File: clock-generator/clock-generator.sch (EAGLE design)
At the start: 100 parts, among them IC1 24C00TS, K2 694108106102, M1 MENTOR_12701001, U1 SN74LVC1G04DBV, U2 ADP151AUJZ, U3 ATSAMD21E, U4 SI5351C, U5 IP4234CZ6, U6 IP4234CZ6, X1 MINI-USB-SHIELD-UX60A-MB-5ST, X2 JACK2.5_SJ-2523, X4 UEXT/90

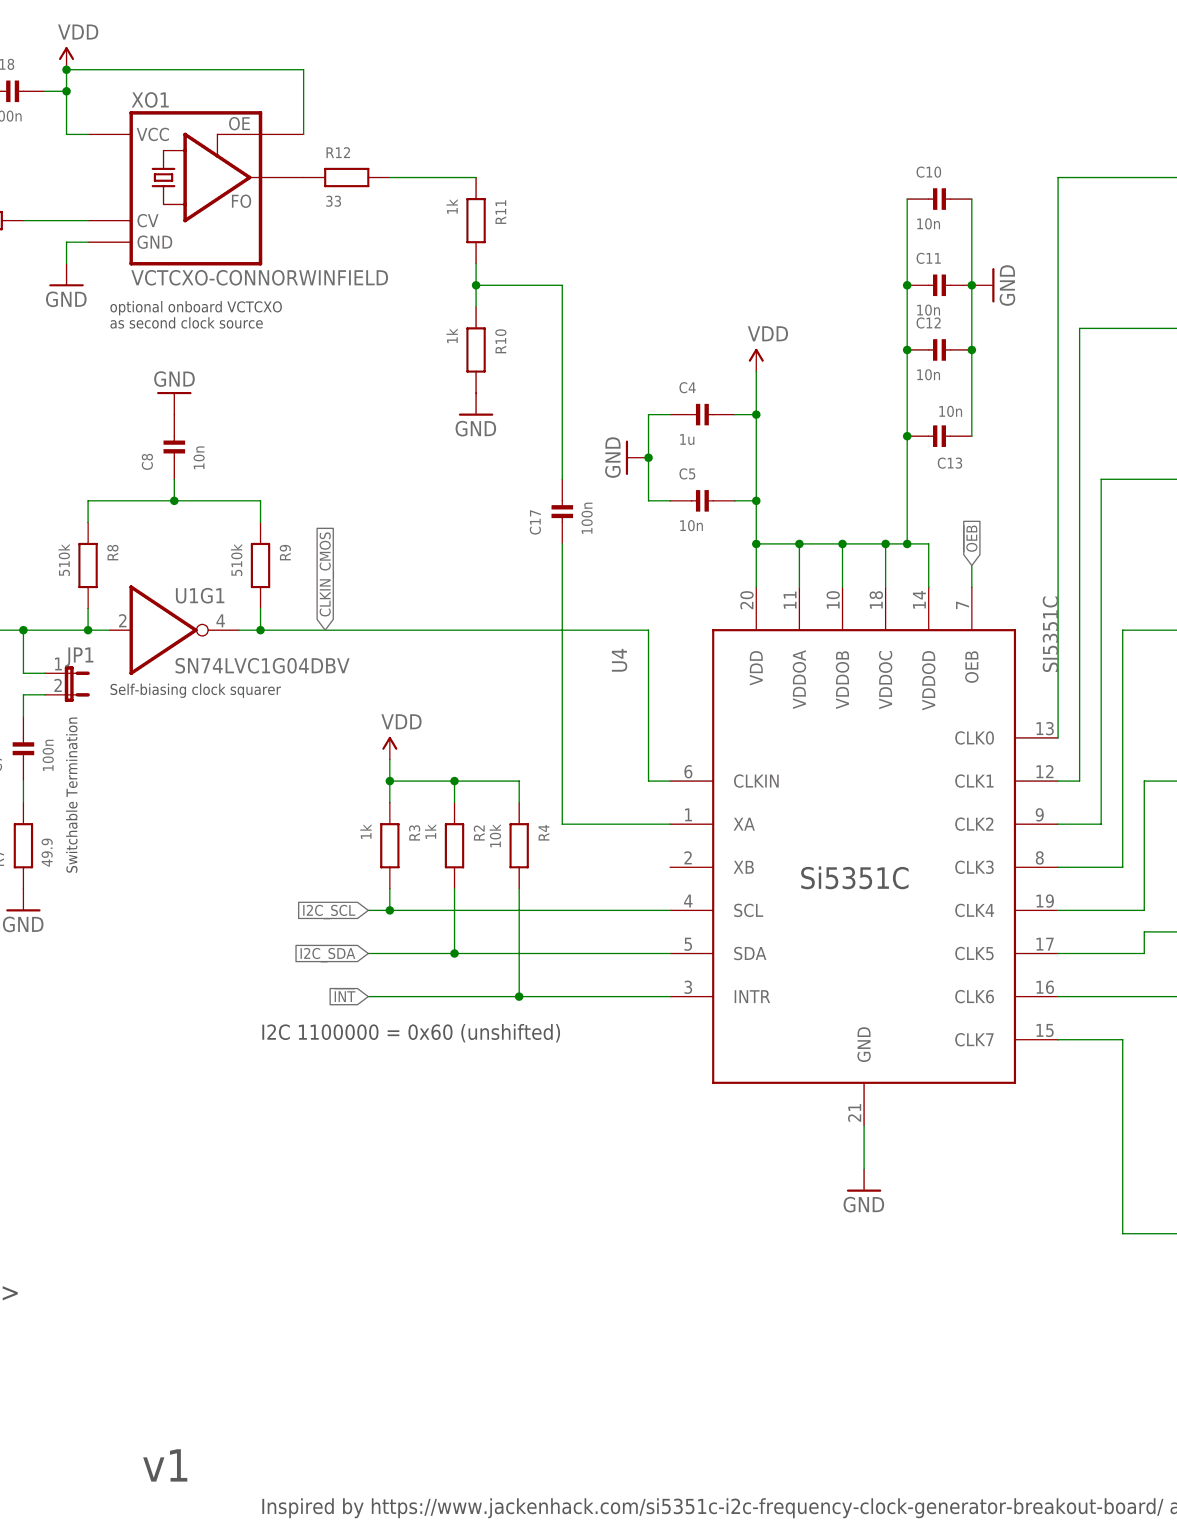
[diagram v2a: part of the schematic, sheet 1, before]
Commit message: clock-generator: add tracking LDO, make PCB four layer
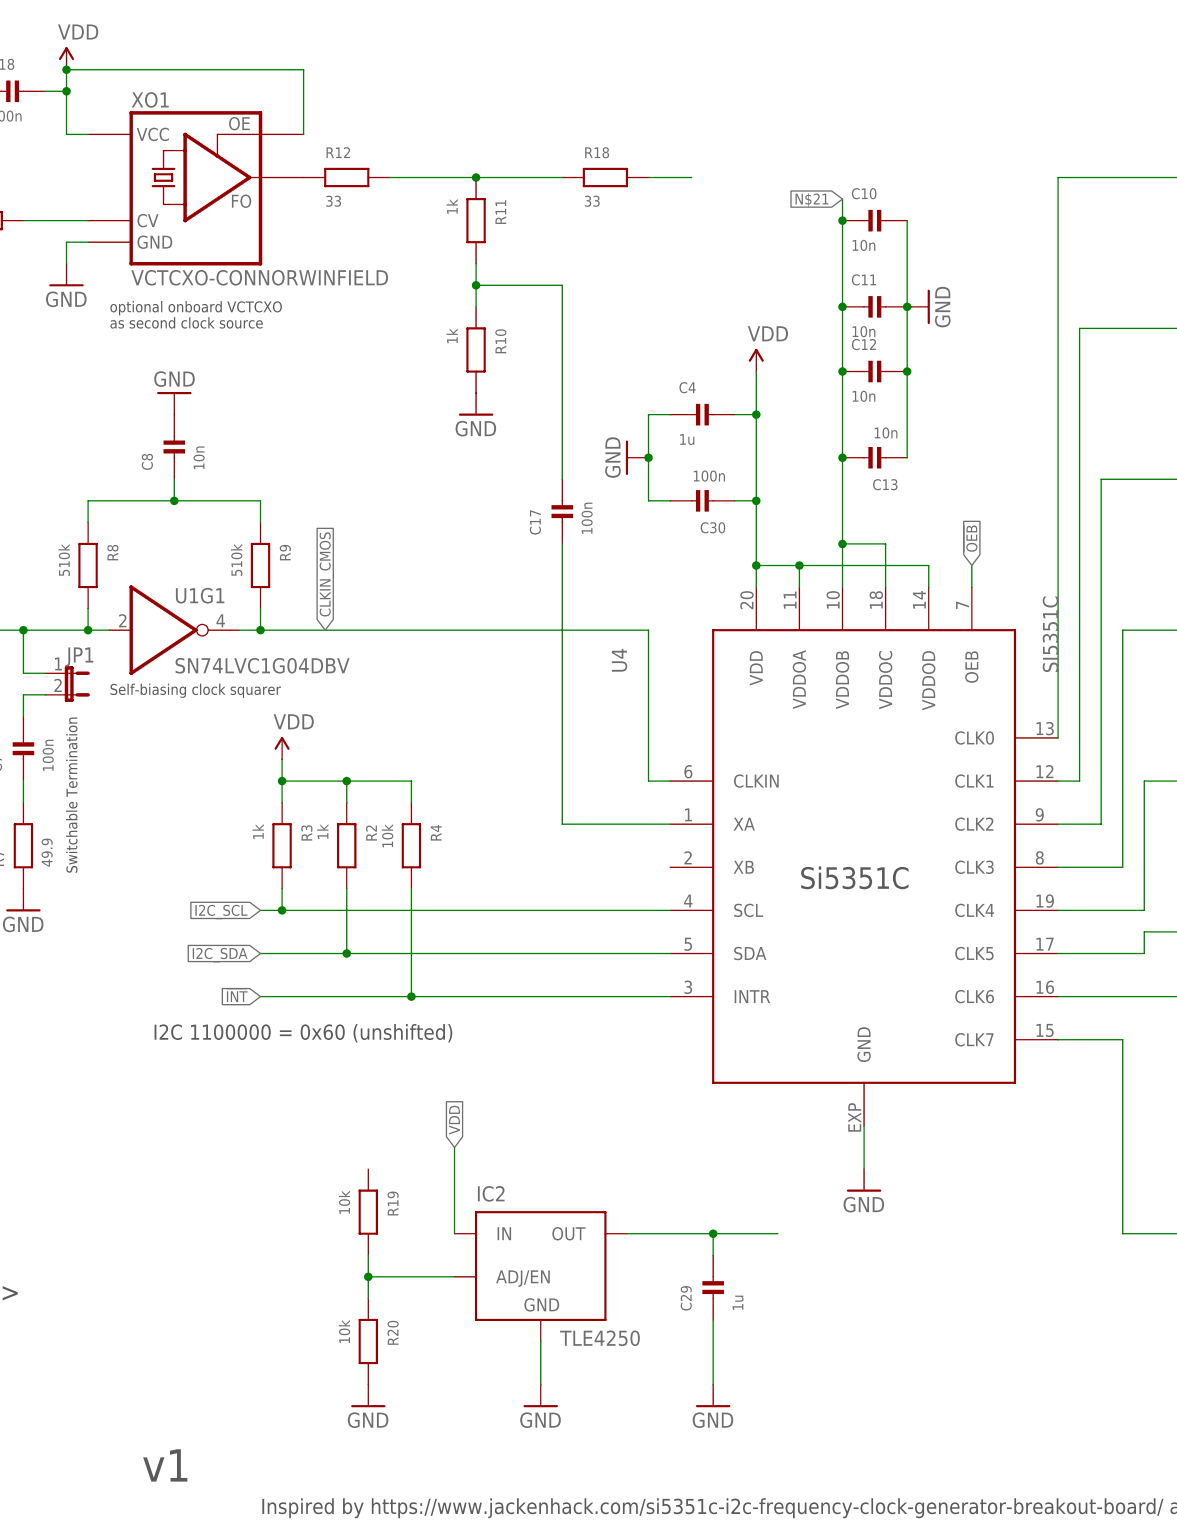
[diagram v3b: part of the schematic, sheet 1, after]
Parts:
- removed C5: 10n, rc-sysmocom:CAP_CERAMIC_0402
- added C29: 1u, rc-sysmocom:CAP_CERAMIC_0603
- added C30: 100n, rc-sysmocom:CAP_CERAMIC_0603
- added IC2: TLE4250, TLE4250:TLE4250
- added R18: 33, rc-sysmocom:RESISTOR_0603
- added R19, R20: 10k, rc-sysmocom:RESISTOR_0603
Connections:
- new net N$17: R18.2
- new net N$18: U3.PA10/AIN18/X2/SC0P2/SC2P2/TCC1WO0/TCC0WO2/I2S_SCK0/GCLK_IO4
- new net N$19: C29.2, IC2.OUT
- new net N$20: IC2.ADJ/EN, R19.2, R20.1
- new net N$21: C10.1, C11.1, C12.1, C13.2, U4.VDDOB, U4.VDDOC
- new net N$8: U3.PA28/TCC3WO7/GCLK_IO0
- new net UART_RX1: U3.PA01/SC1P1/TCC2WO1, X4.RXD
- new net UART_TX1: U3.PA00/SC1P0/TCC2WO0, X4.TXD
- net GND: now also C29.1, C30.2, IC2.GND, R20.2; no longer C5.1
- net N$1: now also R18.1
- net SWCLK: no longer U3.PA30/SC1P2/TCC1WO0/TCC3WO4/SWCLK/GCLK_IO0
- net UART_RX0: no longer X4.RXD
- net UART_TX0: no longer X4.TXD
- net VDD: now also C30.1, IC2.IN; no longer C10.1, C11.1, C12.1, C13.2, C5.2, U4.VDDOB, U4.VDDOC
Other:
- moved on the sheet: C10, C11, C12, C13, R2, R3, R4, U4

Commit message: clock-generator: insert changes discussed so far for v2
* selectable VDDIO{1..4} for PLL: either 3V3 or ADJ (VOUT/DAC)
* use SAMD21 instead of SAMD11
* bring some GPIO on pin header
* use GCLK_IO4 (PA10) to feed XA of PLL
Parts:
- removed C28, C30: 100n, rc-sysmocom:CAP_CERAMIC_0603
- removed C29: 1u, rc-sysmocom:CAP_CERAMIC_0603
- removed C701: 10n, rc-sysmocom:CAP_CERAMIC_0402
- removed CLK0: (no value), laforge:SMA-F-S-TH
- removed K2: 694108106102, Wurth_Elektronik_Electromechanic_DC_Power_Jack_Connectors_rev15c:694108106102
- removed R701, R703: 100k, rc-sysmocom:RESISTOR_0603
- removed XO1: VCTCXO-CONNORWINFIELD, Connor-Winfield_VCTCXO:VCTCXO-CONNORWINFIELD
- added C5: 100n, rc-sysmocom:CAP_CERAMIC_0603
- added CLK8: (no value), laforge:SMA-F-S-TH
- added JP3, JP4, JP5: (no value), pinhead-2:PINHD-1X03_2.54-S
- added JP6: (no value), laforge:PINHD-1X2
- added K1: 694108106102, Wurth_Elektronik_Electromechanic_DC_Power_Jack_Connectors_rev15c:694108106102
- added R21: 0, rc-sysmocom:RESISTOR_0603
- added T1: BC847, transistor:BC847C-NPN-SOT23-BEC
- added X5: UEXT/90, laforge:UEXT/90
- C1: value 4.7u -> 100n; device rc-sysmocom:CAP_CERAMIC_0805 -> rc-sysmocom:CAP_CERAMIC_0603; DESCRIPTION CAP CER 4.7UF 16V X5R 0805 -> CAP CER 0.1UF 16V X7R 0603; LINK https://www.digikey.de/product-detail/de/samsung-electro-mechanics/CL21A475KOFNNNE/1276-1065-1-ND/3889151 -> https://www.digikey.de/product-detail/de/samsung-electro-mechanics/CL10B104KO8NNNC/1276-1005-1-ND/3889091; MANUFACTURERPARTNUMBER CL21A475KOFNNNE -> CL10B104KO8NNNC; SOURCEPARTNUMBER 1276-1065-1-ND -> 1276-1005-1-ND
- C10: value 10n -> 22u; device rc-sysmocom:CAP_CERAMIC_0402 -> rc-sysmocom:CAP_CERAMIC_0805; DESCRIPTION CAP CER 10000PF 25V X7R 0402 -> CAP CER 22UF 6.3V 20% X5R 0805; LINK https://www.digikey.de/product-detail/de/samsung-electro-me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 -> http://www.digikey.de/product-detail/de/CL21A226MQQNNNE/127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; MANUFACTURER Samsung Electro-Mechanics -> Samsung Electro-Mechanics America, Inc; MANUFACTURERPARTNUMBER CL05B103KA5NNNC -> CL21A226MQQNNNE; POPULATED TRUE -> FALSE; SOURCEPARTNUMBER 1276-1057-1-ND -> 1276-1100-1-ND
- C11: value 10n -> 1u; device rc-sysmocom:CAP_CERAMIC_0402 -> rc-sysmocom:CAP_CERAMIC_0603; DESCRIPTION CAP CER 10000PF 25V X7R 0402 -> CAP CER 1UF 10V X5R 0603; LINK https://www.digikey.de/product-detail/de/samsung-electro-mechanics/CL05B103KA5NNNC/1276-1057-1-ND/3889143 -> https://www.digikey.de/product-detail/de/samsung-electro-mechanics/CL10A105KP8NNNC/1276-1182-1-ND/3889268; MANUFACTURERPARTNUMBER CL05B103KA5NNNC -> CL10A105KP8NNNC; SOURCEPARTNUMBER 1276-1057-1-ND -> 1276-1182-1-ND
- C12: value 10n -> 100n; device rc-sysmocom:CAP_CERAMIC_0402 -> rc-sysmocom:CAP_CERAMIC_0603; DESCRIPTION CAP CER 10000PF 25V X7R 0402 -> CAP CER 0.1UF 16V X7R 0603; LINK https://www.digikey.de/product-detail/de/samsung-electro-mechanics/CL05B103KA5NNNC/1276-1057-1-ND/3889143 -> https://www.digikey.de/product-detail/de/samsung-electro-mechanics/CL10B104KO8NNNC/1276-1005-1-ND/3889091; MANUFACTURERPARTNUMBER CL05B103KA5NNNC -> CL10B104KO8NNNC; SOURCEPARTNUMBER 1276-1057-1-ND -> 1276-1005-1-ND
- C13, C8: value 10n -> 100n; DESCRIPTION CAP CER 10000PF 25V X7R 0402 -> NO DESCRIPTION; LINK https://www.digikey.de/product-detail/de/samsung-electro-me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 -> UNKNOWN LINK; MANUFACTURER Samsung Electro-Mechanics -> UNKNOWN MANUFACTURER; MANUFACTURERPARTNUMBER CL05B103KA5NNNC -> UNKNOWN MANUFACTURER PART NUMBER; ROHSCERTIFICATE Bleifrei / RoHS-konform -> UNKNOWN ROHS CERTIFICATE; SOURCE DIGIKEY -> UNKNOWN SOURCE; SOURCEPARTNUMBER 1276-1057-1-ND -> UNKNOWN SOURCE PART NUMBER
- C14, C15: value 4.7u -> 100n; device rc-sysmocom:CAP_CERAMIC_0805 -> rc-sysmocom:CAP_CERAMIC_0402; DESCRIPTION CAP CER 4.7UF 16V X5R 0805 -> NO DESCRIPTION; LINK https://www.digikey.de/product-detail/de/samsung-electro-me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 -> UNKNOWN LINK; MANUFACTURER Samsung Electro-Mechanics -> UNKNOWN MANUFACTURER; MANUFACTURERPARTNUMBER CL21A475KOFNNNE -> UNKNOWN MANUFACTURER PART NUMBER; ROHSCERTIFICATE Bleifrei / RoHS-konform -> UNKNOWN ROHS CERTIFICATE; SOURCE DIGIKEY -> UNKNOWN SOURCE; SOURCEPARTNUMBER 1276-1065-1-ND -> UNKNOWN SOURCE PART NUMBER
- C16, C9: device rc-sysmocom:CAP_CERAMIC_0603 -> rc-sysmocom:CAP_CERAMIC_0402; DESCRIPTION CAP CER 0.1UF 16V X7R 0603 -> NO DESCRIPTION; LINK https://www.digikey.de/product-detail/de/samsung-electro-me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 -> UNKNOWN LINK; MANUFACTURER Samsung Electro-Mechanics -> UNKNOWN MANUFACTURER; MANUFACTURERPARTNUMBER CL10B104KO8NNNC -> UNKNOWN MANUFACTURER PART NUMBER; ROHSCERTIFICATE Bleifrei / RoHS-konform -> UNKNOWN ROHS CERTIFICATE; SOURCE DIGIKEY -> UNKNOWN SOURCE; SOURCEPARTNUMBER 1276-1005-1-ND -> UNKNOWN SOURCE PART NUMBER
- C17, C6, C7: value 100n -> 10n; device rc-sysmocom:CAP_CERAMIC_0603 -> rc-sysmocom:CAP_CERAMIC_0402; DESCRIPTION CAP CER 0.1UF 16V X7R 0603 -> CAP CER 10000PF 25V X7R 0402; LINK https://www.digikey.de/product-detail/de/samsung-electro-mechanics/CL10B104KO8NNNC/1276-1005-1-ND/3889091 -> https://www.digikey.de/product-detail/de/samsung-electro-mechanics/CL05B103KA5NNNC/1276-1057-1-ND/3889143; MANUFACTURERPARTNUMBER CL10B104KO8NNNC -> CL05B103KA5NNNC; SOURCEPARTNUMBER 1276-1005-1-ND -> 1276-1057-1-ND
- C18, C22, C24, C26: value 100n -> 4.7u; device rc-sysmocom:CAP_CERAMIC_0603 -> rc-sysmocom:CAP_CERAMIC_0805; DESCRIPTION CAP CER 0.1UF 16V X7R 0603 -> CAP CER 4.7UF 16V X5R 0805; LINK https://www.digikey.de/product-detail/de/samsung-electro-mechanics/CL10B104KO8NNNC/1276-1005-1-ND/3889091 -> https://www.digikey.de/product-detail/de/samsung-electro-mechanics/CL21A475KOFNNNE/1276-1065-1-ND/3889151; MANUFACTURERPARTNUMBER CL10B104KO8NNNC -> CL21A475KOFNNNE; SOURCEPARTNUMBER 1276-1005-1-ND -> 1276-1065-1-ND
- C20, C25: device rc-sysmocom:CAP_CERAMIC_0603 -> rc-sysmocom:CAP_CERAMIC_0402; DESCRIPTION CAP CER 0.1UF 16V X7R 0603 -> CAP CER 0.1UF 10V X5R 0402; LINK https://www.digikey.de/product-detail/de/samsung-electro-mechanics/CL10B104KO8NNNC/1276-1005-1-ND/3889091 -> https://www.digikey.de/product-detail/de/samsung-electro-mechanics/CL05A104MP5NNNC/1276-1443-1-ND/3889529; MANUFACTURERPARTNUMBER CL10B104KO8NNNC -> CL05A104MP5NNNC; SOURCEPARTNUMBER 1276-1005-1-ND -> 1276-1443-1-ND
- C21, C23: value 100n -> 1u; DESCRIPTION CAP CER 0.1UF 16V X7R 0603 -> CAP CER 1UF 10V X5R 0603; LINK https://www.digikey.de/product-detail/de/samsung-electro-mechanics/CL10B104KO8NNNC/1276-1005-1-ND/3889091 -> https://www.digikey.de/product-detail/de/samsung-electro-mechanics/CL10A105KP8NNNC/1276-1182-1-ND/3889268; MANUFACTURERPARTNUMBER CL10B104KO8NNNC -> CL10A105KP8NNNC; SOURCEPARTNUMBER 1276-1005-1-ND -> 1276-1182-1-ND
- C3: value 100n -> 10n; DESCRIPTION CAP CER 0.1UF 10V X5R 0402 -> CAP CER 10000PF 25V X7R 0402; LINK https://www.digikey.de/product-detail/de/samsung-electro-mechanics/CL05A104MP5NNNC/1276-1443-1-ND/3889529 -> https://www.digikey.de/product-detail/de/samsung-electro-mechanics/CL05B103KA5NNNC/1276-1057-1-ND/3889143; MANUFACTURERPARTNUMBER CL05A104MP5NNNC -> CL05B103KA5NNNC; SOURCEPARTNUMBER 1276-1443-1-ND -> 1276-1057-1-ND
- C4: value 1u -> 10n; device rc-sysmocom:CAP_CERAMIC_0603 -> rc-sysmocom:CAP_CERAMIC_0402; DESCRIPTION CAP CER 1UF 10V X5R 0603 -> CAP CER 10000PF 25V X7R 0402; LINK https://www.digikey.de/product-detail/de/samsung-electro-mechanics/CL10A105KP8NNNC/1276-1182-1-ND/3889268 -> https://www.digikey.de/product-detail/de/samsung-electro-mechanics/CL05B103KA5NNNC/1276-1057-1-ND/3889143; MANUFACTURERPARTNUMBER CL10A105KP8NNNC -> CL05B103KA5NNNC; SOURCEPARTNUMBER 1276-1182-1-ND -> 1276-1057-1-ND
- D10: value 5.6V -> CUS08F30; device diodes-sysmocom:DIODDE-ZENER-SMA -> diodes-sysmocom:DIODE-SCHOTTKY-SOD-323; DESCRIPTION DIODE ZENER 5.6V 3W DO214AC -> DIODE SCHOTTKY 30V 800MA USC; LINK https://www.digikey.de/product-detail/de/micro-commercial-c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 -> https://www.digikey.de/product-detail/de/toshiba-semiconduc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; MANUFACTURER Micro Commercial Co -> Toshiba Semiconductor and Storage; MANUFACTURERPARTNUMBER 3SMAJ5919B-TP -> CUS08F30,H3F; SOURCEPARTNUMBER 3SMAJ5919B-TPMSCT-ND -> CUS08F30H3FCT-ND
- D12: value CUS08F30 -> 5.6V; device diodes-sysmocom:DIODE-SCHOTTKY-SOD-323 -> diodes-sysmocom:DIODDE-ZENER-SMA; DESCRIPTION DIODE SCHOTTKY 30V 800MA USC -> DIODE ZENER 5.6V 3W DO214AC; LINK https://www.digikey.de/product-detail/de/toshiba-semiconduc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 -> https://www.digikey.de/product-detail/de/micro-commercial-c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; MANUFACTURER Toshiba Semiconductor and Storage -> Micro Commercial Co; MANUFACTURERPARTNUMBER CUS08F30,H3F -> 3SMAJ5919B-TP; SOURCEPARTNUMBER CUS08F30H3FCT-ND -> 3SMAJ5919B-TPMSCT-ND
- IC1: value 24C00TS -> TLV9001; device EEPROM-24C0x:24C00TS -> burr-brown:OPA237N; DESCRIPTION IC EEPROM 2K I2C 1MHZ 8TSSOP -> NO DESCRIPTION; LINK https://www.digikey.de/product-detail/de/microchip-technolo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 -> UNKNOWN LINK; MANUFACTURER Microchip Technology -> UNKNOWN MANUFACTURER; MANUFACTURERPARTNUMBER AT24C02C-XHM-T -> UNKNOWN MANUFACTURER PART NUMBER; ROHSCERTIFICATE Bleifrei / RoHS-konform -> UNKNOWN ROHS CERTIFICATE; SOURCE DIGIKEY -> UNKNOWN SOURCE; SOURCEPARTNUMBER AT24C02C-XHM-TCT-ND -> UNKNOWN SOURCE PART NUMBER
- IC2: value TLE4250 -> 24C00TS; device TLE4250:TLE4250 -> EEPROM-24C0x:24C00TS; CLASS (none) -> UNKNOWN CLASS; DESCRIPTION (none) -> IC EEPROM 2K I2C 1MHZ 8TSSOP; LINK (none) -> https://www.digikey.de/product-detail/de/microchip-technolo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; MANUFACTURER (none) -> Microchip Technology; MANUFACTURERPARTNUMBER (none) -> AT24C02C-XHM-T; POPULATED (none) -> TRUE; ROHSCERTIFICATE (none) -> Bleifrei / RoHS-konform; SOURCE (none) -> DIGIKEY; SOURCEPARTNUMBER (none) -> AT24C02C-XHM-TCT-ND
- JP2: device laforge:PINHD-1X2 -> pinhead-2:PINHD-1X03_2.54-S; DESCRIPTION CONN HEADER VERT 2POS 2.54MM -> NO DESCRIPTION; LINK https://www.digikey.de/product-detail/de/PREC002SAAN-RC/S10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 -> UNKNOWN LINK; MANUFACTURER Sullins Connector Solutions -> UNKNOWN MANUFACTURER; MANUFACTURERPARTNUMBER PREC002SAAN-RC -> UNKNOWN MANUFACTURER PART NUMBER; ROHSCERTIFICATE Bleifrei / RoHS-konform -> UNKNOWN ROHS CERTIFICATE; SOURCE DIGIKEY -> UNKNOWN SOURCE; SOURCEPARTNUMBER S1012EC-02-ND -> UNKNOWN SOURCE PART NUMBER
- LED1: value green -> yellow; DESCRIPTION LED GREEN CLEAR 2PLCC SMD -> LED YELLOW CLEAR 2PLCC SMD; LINK https://www.digikey.de/product-detail/de/osram-opto-semiconductors-inc/LG-T67F-R1T1-24/475-3413-1-ND/7908021 -> https://www.digikey.de/product-detail/de/osram-opto-semiconductors-inc/LY-T676-S1T1-26-Z/475-2665-1-ND; MANUFACTURERPARTNUMBER LG T67F-R1T1-24 -> LY T676-S1T1-26-Z; SOURCEPARTNUMBER 475-3413-1-ND -> 475-2665-1-ND
- LED2: value yellow -> green; DESCRIPTION LED YELLOW CLEAR 2PLCC SMD -> LED GREEN CLEAR 2PLCC SMD; LINK https://www.digikey.de/product-detail/de/osram-opto-semiconductors-inc/LY-T676-S1T1-26-Z/475-2665-1-ND -> https://www.digikey.de/product-detail/de/osram-opto-semiconductors-inc/LG-T67F-R1T1-24/475-3413-1-ND/7908021; MANUFACTURERPARTNUMBER LY T676-S1T1-26-Z -> LG T67F-R1T1-24; SOURCEPARTNUMBER 475-2665-1-ND -> 475-3413-1-ND
- R1: value 100k -> 10k; DESCRIPTION RES SMD 100K OHM 5%% 1/10W 0603 -> RES 10K OHM 5%% 1/10W 0603; LINK https://www.digikey.de/product-detail/de/yageo/RC0603JR-071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 -> https://www.digikey.de/product-detail/de/stackpole-electron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; MANUFACTURER Yageo -> Stackpole Electronics Inc.; MANUFACTURERPARTNUMBER RC0603JR-07100KL -> RMCF0603JT10K0; SOURCEPARTNUMBER 311-100KGRCT-ND -> RMCF0603JT10K0CT-ND
- R10, R11: value 1k -> 100k; DESCRIPTION RES 1K OHM 1%% 1/10W 0603 -> RES SMD 100K OHM 5%% 1/10W 0603; LINK https://www.digikey.de/product-detail/de/stackpole-electron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 -> https://www.digikey.de/product-detail/de/yageo/RC0603JR-071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; MANUFACTURER Stackpole Electronics Inc. -> Yageo; MANUFACTURERPARTNUMBER RMCF0603FT1K00 -> RC0603JR-07100KL; SOURCEPARTNUMBER RMCF0603FT1K00CT-ND -> 311-100KGRCT-ND
- R12, R15, R18: value 33 -> 100k; DESCRIPTION RES 33 OHM 5%% 1/10W 0603 -> RES SMD 100K OHM 5%% 1/10W 0603; LINK https://www.digikey.de/product-detail/de/stackpole-electron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 -> https://www.digikey.de/product-detail/de/yageo/RC0603JR-071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; MANUFACTURER Stackpole Electronics Inc. -> Yageo; MANUFACTURERPARTNUMBER RMCF0603JT33R0 -> RC0603JR-07100KL; SOURCEPARTNUMBER RMCF0603JT33R0CT-ND -> 311-100KGRCT-ND
- R13: value 330 -> 30k; DESCRIPTION RES 330 OHM 5%% 1/10W 0603 -> RES SMD 30K OHM 5%% 1/10W 0603; LINK https://www.digikey.de/product-detail/de/stackpole-electron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 -> https://www.digikey.de/product-detail/de/yageo/RC0603JR-073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; MANUFACTURER Stackpole Electronics Inc. -> Yageo; MANUFACTURERPARTNUMBER RMCF0603JT330R -> RC0603JR-0730KL; SOURCEPARTNUMBER RMCF0603JT330RCT-ND -> 311-30KGRCT-ND
- R14: value 330 -> 47k; DESCRIPTION RES 330 OHM 5%% 1/10W 0603 -> RES SMD 47K OHM 5%% 1/10W 0603; LINK https://www.digikey.de/product-detail/de/stackpole-electron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 -> https://www.digikey.de/product-detail/de/yageo/RC0603JR-074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; MANUFACTURER Stackpole Electronics Inc. -> Yageo; MANUFACTURERPARTNUMBER RMCF0603JT330R -> RC0603JR-0747KL; SOURCEPARTNUMBER RMCF0603JT330RCT-ND -> 311-47KGRCT-ND
- R16: value 30k -> 330; DESCRIPTION RES SMD 30K OHM 5%% 1/10W 0603 -> RES 330 OHM 5%% 1/10W 0603; LINK https://www.digikey.de/product-detail/de/yageo/RC0603JR-073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 -> https://www.digikey.de/product-detail/de/stackpole-electron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; MANUFACTURER Yageo -> Stackpole Electronics Inc.; MANUFACTURERPARTNUMBER RC0603JR-0730KL -> RMCF0603JT330R; SOURCEPARTNUMBER 311-30KGRCT-ND -> RMCF0603JT330RCT-ND
- R17: value 47k -> 330; DESCRIPTION RES SMD 47K OHM 5%% 1/10W 0603 -> RES 330 OHM 5%% 1/10W 0603; LINK https://www.digikey.de/product-detail/de/yageo/RC0603JR-074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 -> https://www.digikey.de/product-detail/de/stackpole-electron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; MANUFACTURER Yageo -> Stackpole Electronics Inc.; MANUFACTURERPARTNUMBER RC0603JR-0747KL -> RMCF0603JT330R; SOURCEPARTNUMBER 311-47KGRCT-ND -> RMCF0603JT330RCT-ND
- R19: value 10k -> 30k; DESCRIPTION RES 10K OHM 5%% 1/10W 0603 -> RES SMD 30K OHM 5%% 1/10W 0603; LINK https://www.digikey.de/product-detail/de/stackpole-electron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 -> https://www.digikey.de/product-detail/de/yageo/RC0603JR-073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; MANUFACTURER Stackpole Electronics Inc. -> Yageo; MANUFACTURERPARTNUMBER RMCF0603JT10K0 -> RC0603JR-0730KL; SOURCEPARTNUMBER RMCF0603JT10K0CT-ND -> 311-30KGRCT-ND
- R2: value 1k -> 10k; DESCRIPTION RES 1K OHM 1%% 1/10W 0603 -> RES 10K OHM 5%% 1/10W 0603; LINK https://www.digikey.de/product-detail/de/stackpole-electronics-inc/RMCF0603FT1K00/RMCF0603FT1K00CT-ND/1942996 -> https://www.digikey.de/product-detail/de/stackpole-electronics-inc/RMCF0603JT10K0/RMCF0603JT10K0CT-ND/1943191; MANUFACTURERPARTNUMBER RMCF0603FT1K00 -> RMCF0603JT10K0; SOURCEPARTNUMBER RMCF0603FT1K00CT-ND -> RMCF0603JT10K0CT-ND
- R20: value 10k -> 47k; DESCRIPTION RES 10K OHM 5%% 1/10W 0603 -> RES SMD 47K OHM 5%% 1/10W 0603; LINK https://www.digikey.de/product-detail/de/stackpole-electron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 -> https://www.digikey.de/product-detail/de/yageo/RC0603JR-074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; MANUFACTURER Stackpole Electronics Inc. -> Yageo; MANUFACTURERPARTNUMBER RMCF0603JT10K0 -> RC0603JR-0747KL; SOURCEPARTNUMBER RMCF0603JT10K0CT-ND -> 311-47KGRCT-ND
- R3: value 1k -> 49.9; DESCRIPTION RES 1K OHM 1%% 1/10W 0603 -> RES 49.9 OHM 1%% 1/10W 0603; LINK https://www.digikey.de/product-detail/de/stackpole-electronics-inc/RMCF0603FT1K00/RMCF0603FT1K00CT-ND/1942996 -> https://www.digikey.de/product-detail/de/stackpole-electronics-inc/RMCF0603FT49R9/RMCF0603FT49R9CT-ND/1942956; MANUFACTURERPARTNUMBER RMCF0603FT1K00 -> RMCF0603FT49R9; SOURCEPARTNUMBER RMCF0603FT1K00CT-ND -> RMCF0603FT49R9CT-ND
- R4, R5: value 10k -> 510k; DESCRIPTION RES 10K OHM 5%% 1/10W 0603 -> RES SMD 510K OHM 1%% 1/10W 0603; LINK https://www.digikey.de/product-detail/de/stackpole-electron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 -> https://www.digikey.de/product-detail/de/yageo/RC0603FR-075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; MANUFACTURER Stackpole Electronics Inc. -> Yageo; MANUFACTURERPARTNUMBER RMCF0603JT10K0 -> RC0603FR-07510KL; SOURCEPARTNUMBER RMCF0603JT10K0CT-ND -> 311-510KHRCT-ND
- R6: value 10k -> 1k; DESCRIPTION RES 10K OHM 5%% 1/10W 0603 -> RES 1K OHM 1%% 1/10W 0603; LINK https://www.digikey.de/product-detail/de/stackpole-electronics-inc/RMCF0603JT10K0/RMCF0603JT10K0CT-ND/1943191 -> https://www.digikey.de/product-detail/de/stackpole-electronics-inc/RMCF0603FT1K00/RMCF0603FT1K00CT-ND/1942996; MANUFACTURERPARTNUMBER RMCF0603JT10K0 -> RMCF0603FT1K00; SOURCEPARTNUMBER RMCF0603JT10K0CT-ND -> RMCF0603FT1K00CT-ND
- R7: value 49.9 -> 0; DESCRIPTION RES 49.9 OHM 1%% 1/10W 0603 -> RES 0.0 OHM 1/10W JUMP 0603; LINK https://www.digikey.de/product-detail/de/stackpole-electron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 -> http://www.digikey.de/product-detail/de/foo/1276-3510-1-ND; MANUFACTURER Stackpole Electronics Inc. -> Samsung Electro-Mechanics America, Inc; MANUFACTURERPARTNUMBER RMCF0603FT49R9 -> RC1608J000CS; SOURCEPARTNUMBER RMCF0603FT49R9CT-ND -> 1276-3510-1-ND
- R8: value 510k -> 1k; DESCRIPTION RES SMD 510K OHM 1%% 1/10W 0603 -> RES 1K OHM 1%% 1/10W 0603; LINK https://www.digikey.de/product-detail/de/yageo/RC0603FR-075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 -> https://www.digikey.de/product-detail/de/stackpole-electron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; MANUFACTURER Yageo -> Stackpole Electronics Inc.; MANUFACTURERPARTNUMBER RC0603FR-07510KL -> RMCF0603FT1K00; SOURCEPARTNUMBER 311-510KHRCT-ND -> RMCF0603FT1K00CT-ND
- R9: value 510k -> 10k; DESCRIPTION RES SMD 510K OHM 1%% 1/10W 0603 -> RES 10K OHM 5%% 1/10W 0603; LINK https://www.digikey.de/product-detail/de/yageo/RC0603FR-075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 -> https://www.digikey.de/product-detail/de/stackpole-electron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; MANUFACTURER Yageo -> Stackpole Electronics Inc.; MANUFACTURERPARTNUMBER RC0603FR-07510KL -> RMCF0603JT10K0; SOURCEPARTNUMBER 311-510KHRCT-ND -> RMCF0603JT10K0CT-ND
- U2: value ADP151AUJZ -> SI5351C; device ldo:LDO_FIXED_EN-ADP151AUJZ -> jackens:SI5351C; DESCRIPTION IC REG LINEAR 3V 200MA TSOT5 -> IC CLK GENERATOR 200MHZ 20QFN; LINK https://www.digikey.de/product-detail/de/analog-devices-inc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 -> https://www.digikey.de/product-detail/de/silicon-labs/SI535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; MANUFACTURER Analog Devices Inc. -> Silicon Labs; MANUFACTURERPARTNUMBER ADP151AUJZ-3.0-R7 -> SI5351C-B-GMR; SOURCEPARTNUMBER ADP151AUJZ-3.0-R7CT-ND -> 336-5160-6-ND
- U3: value ATSAMD21E -> IP4234CZ6; device atmel-arm:ATSAMD21E -> laforge:IP4234CZ6; CLASS (none) -> IC; DESCRIPTION (none) -> TVS DIODE 5.5V 6TSOP; LINK (none) -> https://www.digikey.de/product-detail/de/nexperia-usa-inc/I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; MANUFACTURER (none) -> Nexperia USA Inc.; MANUFACTURERPARTNUMBER (none) -> IP4234CZ6,125; POPULATED (none) -> TRUE; ROHSCERTIFICATE (none) -> Bleifrei / RoHS-konform; SOURCE (none) -> DIGIKEY; SOURCEPARTNUMBER (none) -> 1727-4717-1-ND
- U4: value SI5351C -> ATSAMD21E; device jackens:SI5351C -> atmel-arm:ATSAMD21E; DESCRIPTION IC CLK GENERATOR 200MHZ 20QFN -> IC REG LINEAR 3.3V 200MA TSOT5; LINK https://www.digikey.de/product-detail/de/silicon-labs/SI535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 -> https://www.digikey.de/product-detail/de/analog-devices-inc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; MANUFACTURER Silicon Labs -> Analog Devices Inc.; MANUFACTURERPARTNUMBER SI5351C-B-GMR -> ADP151AUJZ-3.3-R7; SOURCEPARTNUMBER 336-5160-6-ND -> ADP151AUJZ-3.3-R7CT-ND
- U5: value IP4234CZ6 -> ADP151AUJZ; device laforge:IP4234CZ6 -> ldo:LDO_FIXED_EN-ADP151AUJZ; DESCRIPTION TVS DIODE 5.5V 6TSOP -> IC REG LINEAR 3V 200MA TSOT5; LINK https://www.digikey.de/product-detail/de/nexperia-usa-inc/I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 -> https://www.digikey.de/product-detail/de/analog-devices-inc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; MANUFACTURER Nexperia USA Inc. -> Analog Devices Inc.; MANUFACTURERPARTNUMBER IP4234CZ6,125 -> ADP151AUJZ-3.0-R7; SOURCEPARTNUMBER 1727-4717-1-ND -> ADP151AUJZ-3.0-R7CT-ND
- X2: value JACK2.5_SJ-2523 -> (none); device laforge:JACK2.5_SJ-2523 -> SparkFun-Connectors:M05LOCK; DESCRIPTION CONN JACK STEREO 2.5MM SMD R/A -> NO DESCRIPTION; LINK https://www.digikey.de/product-detail/de/cui-inc/SJ-2523-SM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 -> UNKNOWN LINK; MANUFACTURER CUI Inc. -> UNKNOWN MANUFACTURER; MANUFACTURERPARTNUMBER SJ-2523-SMT-TR -> UNKNOWN MANUFACTURER PART NUMBER; ROHSCERTIFICATE Bleifrei / RoHS-konform -> UNKNOWN ROHS CERTIFICATE; SOURCE DIGIKEY -> UNKNOWN SOURCE; SOURCEPARTNUMBER CP-2523SJCT-ND -> UNKNOWN SOURCE PART NUMBER
- X4: value UEXT/90 -> JACK2.5_SJ-2523; device laforge:UEXT/90 -> laforge:JACK2.5_SJ-2523; DESCRIPTION CONN HEADER VERT 10POS 2.54MM -> CONN JACK STEREO 2.5MM SMD R/A; LINK https://www.digikey.de/product-detail/de/on-shore-technolog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 -> https://www.digikey.de/product-detail/de/cui-inc/SJ-2523-SM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; MANUFACTURER On Shore Technology Inc. -> CUI Inc.; MANUFACTURERPARTNUMBER 302-S101 -> SJ-2523-SMT-TR; SOURCEPARTNUMBER ED1543-ND -> CP-2523SJCT-ND
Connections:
- removed net N$10: R15.2, XO1.CV
- removed net N$14: C1.2, D10.C, F1.1, U2.EN, U2.IN
- removed net N$17: R18.2
- removed net N$18: U3.PA10/AIN18/X2/SC0P2/SC2P2/TCC1WO0/TCC0WO2/I2S_SCK0/GCLK_IO4
- removed net N$19: C29.2, IC2.OUT
- removed net N$20: IC2.ADJ/EN, R19.2, R20.1
- removed net N$8: U3.PA28/TCC3WO7/GCLK_IO0
- removed net VCXO_CV: R15.1, U3.PA02/AIN0/Y0/VOUT/TCC3WO0
- new net DAC_VIO: R7.2, U4.PA02/AIN0/Y0/VOUT/TCC3WO0
- new net N$23: IC1.OUT, T1.B
- new net PA11: U4.PA11/AIN19/X3/SC0P3/SC2P3/TCC1WO1/TCC0WO3/I2S_FS0/GCLK_IO5, X2.2
- new net PA14: U4.PA14/SC2P2/SC4P2/TC3WO0/TCC0WO4/GCLK_IO0, X2.3
- new net PA15: U4.PA15/SC2P3/SC4P3/TC3WO1/TCC0WO5/GCLK_IO1, X2.4
- new net VDDIO_ADJ: C10.2, C9.2, IC1.-IN, JP2.3, JP3.3, JP4.3, JP5.3, T1.E
- new net VDDOA: C16.1, JP2.2, U2.VDDOA
- new net VDDOB: C15.1, JP3.2, U2.VDDOB
- new net VDDOC: C14.1, JP4.2, U2.VDDOC
- new net VDDOD: C13.1, JP5.2, U2.VDDOD
- new net V_IN: C18.2, D12.C, F1.1, T1.C, U5.EN, U5.IN
- net !INT: now also R9.2, U2.INTR, U4.PA03/ADCVREFA/DACVREFA/AIN1/Y1/TCC3WO1; no longer R4.2, U3.PA03/ADCVREFA/DACVREFA/AIN1/Y1/TCC3WO1, U4.INTR
- net !LED_YELLOW: now also LED1.C, U4.PA16/X4/SC1P0/SC3P0/TCC2WO0/TCC0WO6/GCLK_IO2; no longer LED2.C, U3.PA16/X4/SC1P0/SC3P0/TCC2WO0/TCC0WO6/GCLK_IO2
- net !OEB: now also U2.OEB, U4.PA17/X5/SC1P1/SC3P1/TCC2WO1/TCC0WO7/GCLK_IO3; no longer U3.PA17/X5/SC1P1/SC3P1/TCC2WO1/TCC0WO7/GCLK_IO3, U4.OEB
- net !RESET: now also R15.2, U4.!RESET; no longer U3.!RESET
- net !SPI_SS: now also U4.PA05/AIN5/AIN1/Y3/SC0P1/TC0WO1/TCC3WO3, X5.SSEL; no longer U3.PA05/AIN5/AIN1/Y3/SC0P1/TC0WO1/TCC3WO3, X4.SSEL
- net CLK0_LINE: now also CLK1.1, D2.K, U2.CLK0; no longer CLK0.1, D1.K, U4.CLK0
- net CLK1_LINE: now also CLK2.1, D3.K, U2.CLK1; no longer CLK1.1, D2.K, U4.CLK1
- net CLK2_LINE: now also CLK3.1, D4.K, U2.CLK2; no longer CLK2.1, D3.K, U4.CLK2
- net CLK3_LINE: now also CLK4.1, D5.K, U2.CLK3; no longer CLK3.1, D4.K, U4.CLK3
- net CLK4_LINE: now also CLK5.1, D6.K, U2.CLK4; no longer CLK4.1, D5.K, U4.CLK4
- net CLK5_LINE: now also CLK6.1, D7.K, U2.CLK5; no longer CLK5.1, D6.K, U4.CLK5
- net CLK6_LINE: now also CLK7.1, D8.K, U2.CLK6; no longer CLK6.1, D7.K, U4.CLK6
- net CLK7_LINE: now also CLK8.1, D9.K, U2.CLK7; no longer CLK7.1, D8.K, U4.CLK7
- net CLKIN: now also C2.1; no longer C6.1
- net CLKIN_AC: now also C2.2, D1.K, R1.1, R2.2, R4.2; no longer C6.2, D9.K, R5.1, R6.2, R8.2
- net CLKIN_CMOS: now also R5.2, U2.CLKIN; no longer R9.2, U4.CLKIN
- net GND: now also C10.1, C11.1, C13.2, C14.2, C15.2, C16.2, C17.2, C19.2, C6.2, C7.1, C8.1, CLK8.GND@1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; no longer C10.2, C11.2, C13.1, C14.1, C15.1, C16.1, C19.1, C2.2, C29.1, C30.2, C701.2, C8.2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
- net I2C_SCL: now also IC2.SCL, R6.2, U2.SCL, U4.PA09/AIN17/X1/SC0P1/SC2P1/TCC0WO1/TCC1WO3/I2S_MCK, X5.SCL; no longer IC1.SCL, R3.2, U3.PA09/AIN17/X1/SC0P1/SC2P1/TCC0WO1/TCC1WO3/I2S_MCK, U4.SCL, X4.SCL
- net I2C_SDA: now also IC2.SDA, R8.2, U2.SDA, U4.PA08/NMI/AIN16/X0/SC0P0/SC2P0/TCC0WO0/TCC1WO2/I2S_SD1, X5.SDA; no longer IC1.SDA, R2.2, U3.PA08/NMI/AIN16/X0/SC0P0/SC2P0/TCC0WO0/TCC1WO2/I2S_SD1, U4.SDA, X4.SDA
- net N$1: now also C21.2, U4.VDDCORE; no longer R11.1, R12.2, R18.1
- net N$11: now also LED2.A, R17.1; no longer LED1.A, R13.1
- net N$12: now also LED1.A, R16.1; no longer LED2.A, R14.1
- net N$13: now also C25.2, C26.2, U4.VDDANA; no longer C15.2, C3.2
- net N$15: now also D10.A, JP6.1, K1.1; no longer D11.A, JP2.1, K2.1
- net N$2: now also R20.1, R21.1; no longer C17.2, R10.1, R11.2
- net N$21: now also C7.2, IC1.+IN, R10.2, R7.1; no longer C10.1, C11.1, C12.1, C13.2, U4.VDDOB, U4.VDDOC
- net N$3: now also C5.1, R3.2; no longer C7.1, R7.2
- net N$4: now also R19.1, R20.2, U2.XA; no longer R12.1, XO1.FO
- net N$5: now also C6.1, R4.1, R5.1; no longer C8.1, R8.1, R9.1
- net N$55: now also R11.1, R12.2; no longer R701.1, R703.2
- net N$6: now also D10.C; no longer D12.C
- net N$61: now also C17.1, R11.2; no longer C701.1, R701.2
- net N$7: now also C5.2; no longer C7.2
- net SPI_MISO: now also U4.PA04/ADCVREFB/AIN4/AIN0/Y2/SC0P0/TCC0WO0/TCC3WO2, X5.MISO; no longer U3.PA04/ADCVREFB/AIN4/AIN0/Y2/SC0P0/TCC0WO0/TCC3WO2, X4.MISO
- net SPI_MOSI: now also U4.PA06/AIN6/AIN2/Y4/SC0P2/TCC1WO0/TCC3WO4, X5.MOSI; no longer U3.PA06/AIN6/AIN2/Y4/SC0P2/TCC1WO0/TCC3WO4, X4.MOSI
- net SPI_SCK: now also U4.PA07/AIN7/AIN3/Y5/SC0P3/TCC1WO1/TCC3WO5/I2S_SD0, X5.SCK; no longer U3.PA07/AIN7/AIN3/Y5/SC0P3/TCC1WO1/TCC3WO5/I2S_SD0, X4.SCK
- net SWCLK: now also U4.PA30/SC1P2/TCC1WO0/TCC3WO4/SWCLK/GCLK_IO0
- net SWDIO: now also U4.PA31/SC1P3/TCC1WO1/TCC3WO5/SWDIO; no longer U3.PA31/SC1P3/TCC1WO1/TCC3WO5/SWDIO
- net UART_RX: now also R18.1, U4.PA23/X11/SC3P1/SC5P1/TC4WO1/TCC0WO5/USB_SOF/GCLK_IO7; no longer R1.1, U3.PA23/X11/SC3P1/SC5P1/TC4WO1/TCC0WO5/USB_SOF/GCLK_IO7
- net UART_RX0: now also X4.TIP; no longer X2.TIP
- net UART_RX1: now also U4.PA01/SC1P1/TCC2WO1, X5.RXD; no longer U3.PA01/SC1P1/TCC2WO1, X4.RXD
- net UART_TX: now also U4.PA22/X10/SC3P0/SC5P0/TC4WO0/TCC0WO4/GCLK_IO6; no longer U3.PA22/X10/SC3P0/SC5P0/TC4WO0/TCC0WO4/GCLK_IO6
- net UART_TX0: now also X4.MIDDLE; no longer X2.MIDDLE
- net UART_TX1: now also U4.PA00/SC1P0/TCC2WO0, X5.TXD; no longer U3.PA00/SC1P0/TCC2WO0, X4.TXD
- net USB0_D_N: now also U3.2A; no longer U5.2A
- net USB0_D_P: now also U3.1A; no longer U5.1A
- net USB1_D_N: now also U3.2B; no longer U5.2B
- net USB1_D_P: now also U3.1B; no longer U5.1B
- net USB_D_N: now also U4.PA24/SC3P2/SC5P2/TC5WO0/TCC1WO2/USB_DM; no longer U3.PA24/SC3P2/SC5P2/TC5WO0/TCC1WO2/USB_DM
- net USB_D_P: now also U4.PA25/SC3P3/SC5P3/TC5WO1/TCC1WO3/USB_DP; no longer U3.PA25/SC3P3/SC5P3/TC5WO1/TCC1WO3/USB_DP
- net VBUS: now also D11.A, R13.2, U3.VCC; no longer D12.A, R16.2, U5.VCC
- net VBUS_DET: now also R13.1, R14.2, U4.PA27/TCC3WO6/GCLK_IO0; no longer R16.1, R17.2, U3.PA27/TCC3WO6/GCLK_IO0
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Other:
- note added: "Stitching Capacitors where clock crosses layers"
- note added: "connectors"
- note added: "microcontroller"
- note added: "power supply"
- note removed: "Connectors"
- note removed: "Microcontroller"
- note removed: "Power Supply"
- note removed: "Stitching Capacitors next to each SMA jack as bottom/reference plane is VCC"
- note removed: "Stitching Capacitors where clock crosses VCC"
- note removed: "optional onboard VCTCXO as second clock source"
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
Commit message: clock-generator: changes adressing OSM#4050
A shouded UEXT would need much space; no room for an MTA100 yet... tbd
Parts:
- removed TC1: TC2030-IDC, tag-connect:TC2030-IDC
- added J1: (no value), con-amp:MTA02-100
- added JP7: M05X2SHD, SparkFun-Connectors:M05X2SHD
- added TC501: TC2050-IDC, tag-connect:TC2050-IDC
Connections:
- new net VDD_3V3: TC501.4
- net !RESET: now also TC501.6; no longer TC1.4
- net GND: now also TC501.10, TC501.2; no longer TC1.3
- net SWCLK: now also TC501.1; no longer TC1.6
- net SWDIO: now also TC501.5; no longer TC1.5
- net UART_RX: no longer TC1.2
- net UART_TX: no longer TC1.1
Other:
- note added: "2x5pin TagConnect SWD"
- note added: "Tag-Connect TC-2050 connector for SWD Flashing/Debugging"
- note removed: "Tag-Connect TC-2030 connector for SWD Flashing/Debugging"
- moved on the sheet: R18, U6, X3, X4

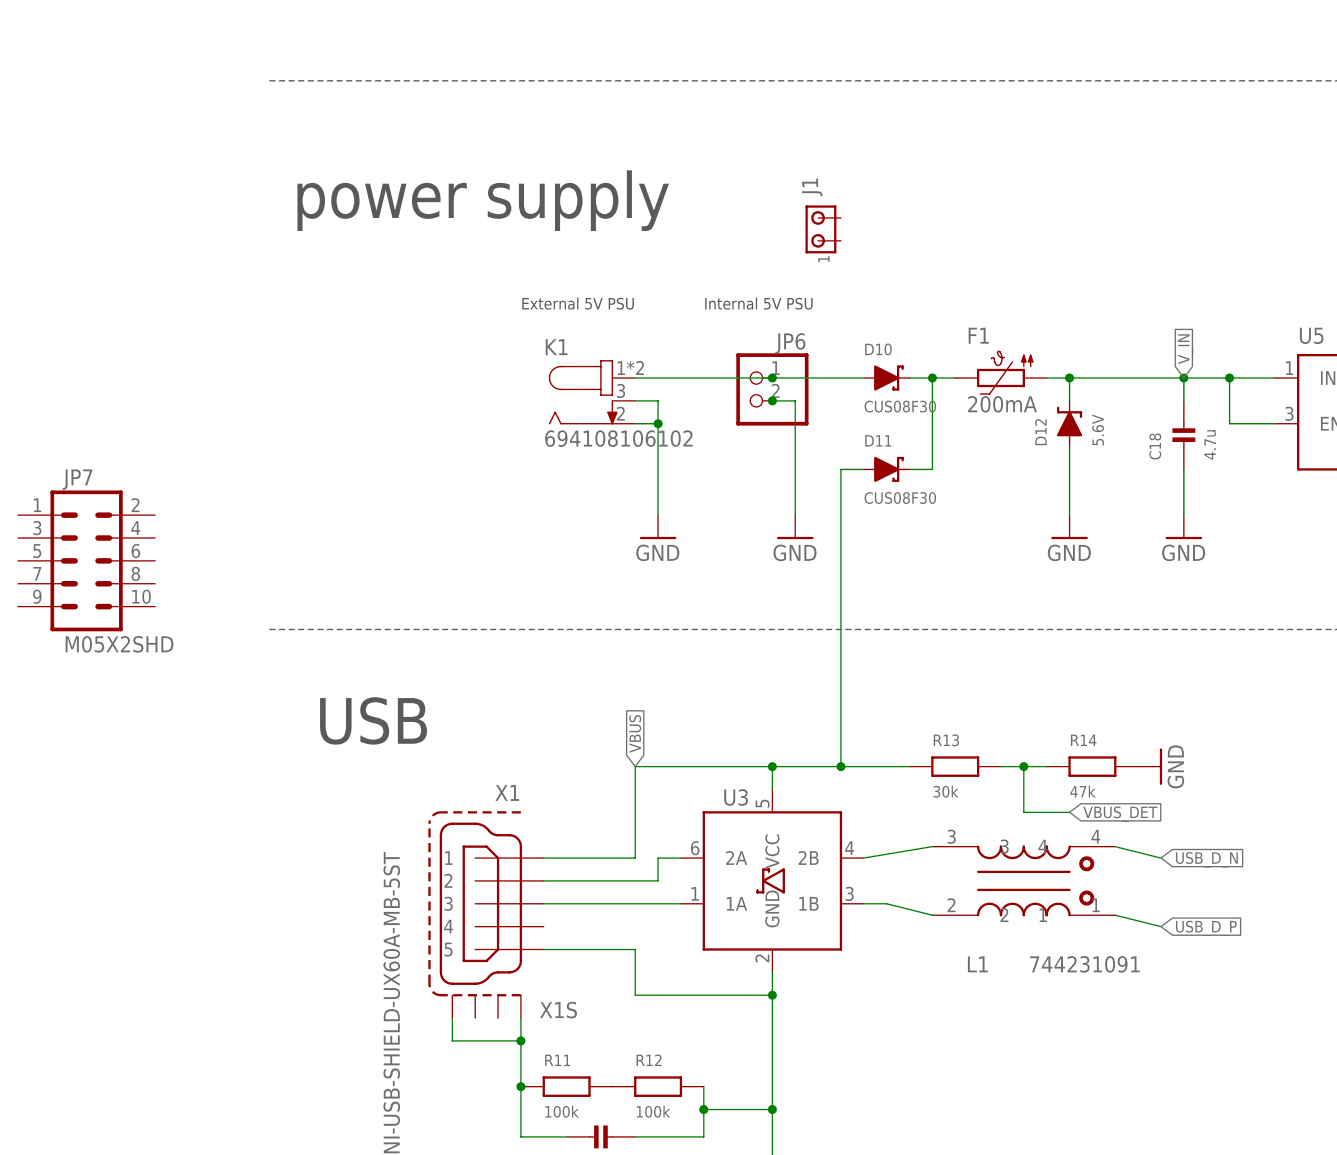
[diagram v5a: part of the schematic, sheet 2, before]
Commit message: clock-generator: compacting + place MTA100 header (solves OSM#4050)
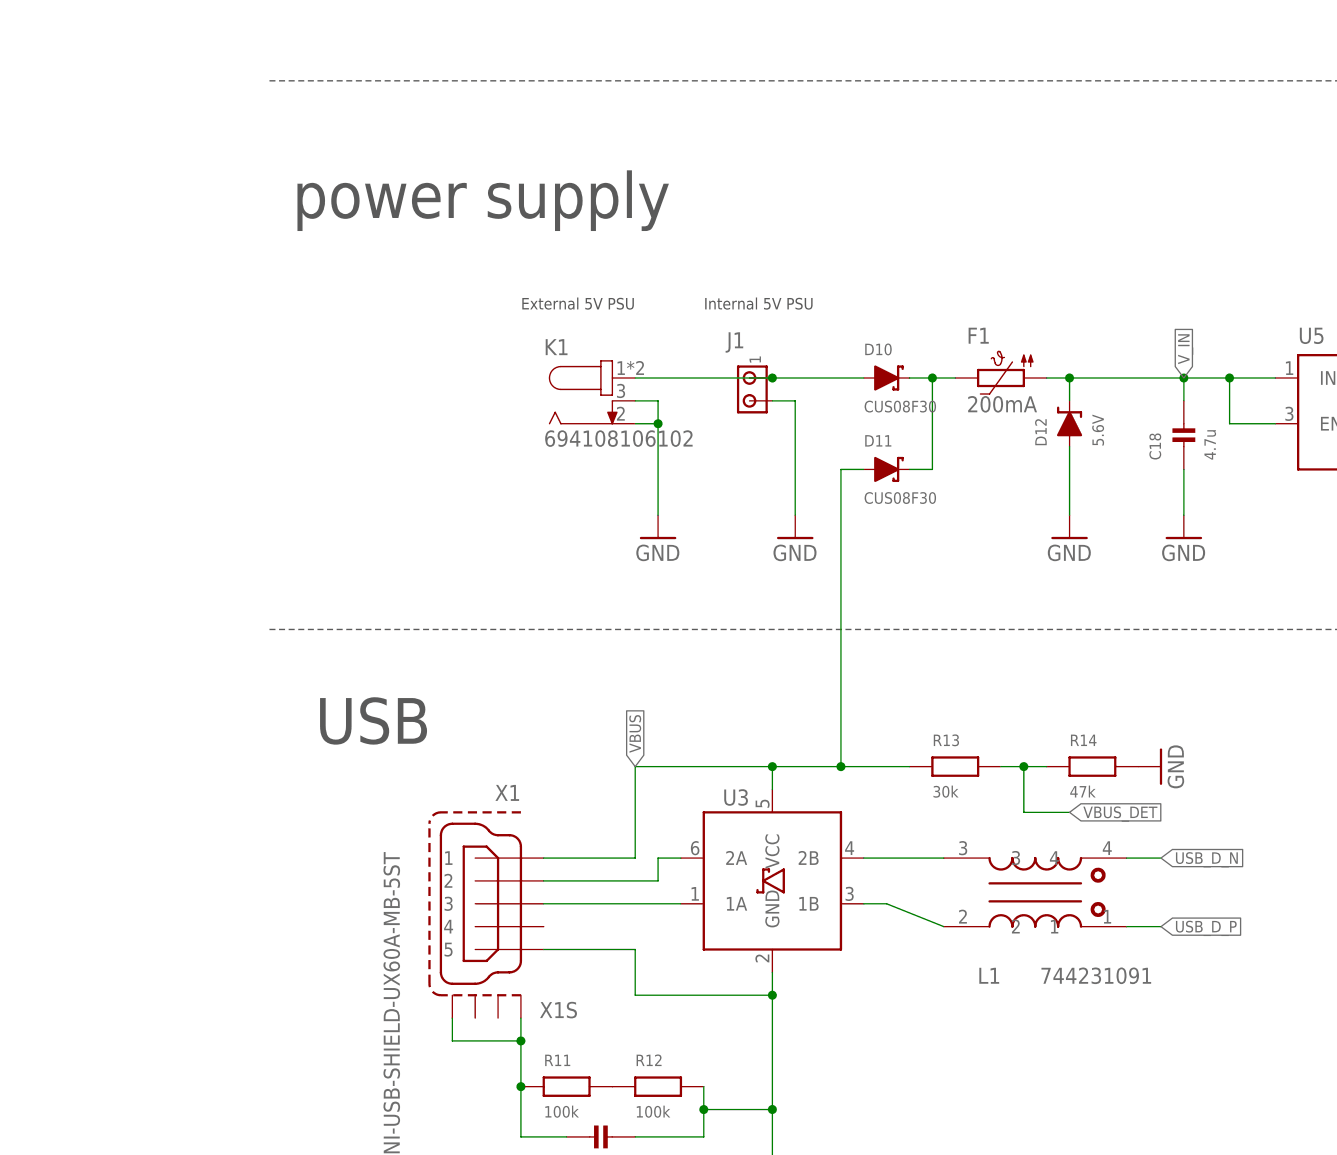
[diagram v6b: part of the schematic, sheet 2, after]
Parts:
- removed JP6: (no value), laforge:PINHD-1X2
- removed JP7: M05X2SHD, SparkFun-Connectors:M05X2SHD
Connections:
- net GND: now also J1.2; no longer JP6.2
- net N$15: now also J1.1; no longer JP6.1
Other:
- moved on the sheet: J1, L1
